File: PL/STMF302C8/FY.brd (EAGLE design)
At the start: 70 x 69 mm, 51 parts, among them J1 CON-SD-CARD_MICROSD-2908-05, J2 Flash Programming, U1 AS72652-BLGT, U2 AS72653-BLGT, U3 STM32F302C8T6, U4 AS72651-BLGT, U5 AMS1117-3.3, U6 4MB Flash, Y2 ABM2B-8.000MHZ-10-1-U-T

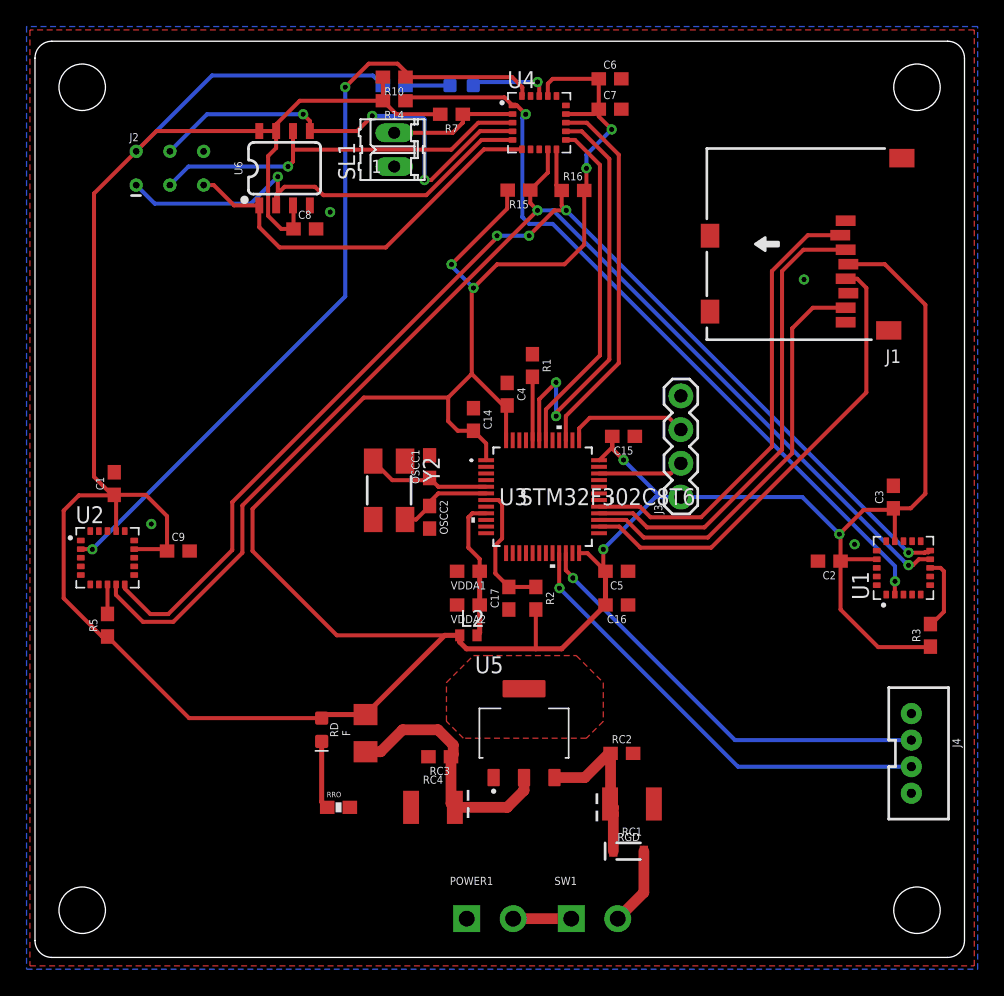
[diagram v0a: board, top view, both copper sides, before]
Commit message: Connector was changed and Preparing first order
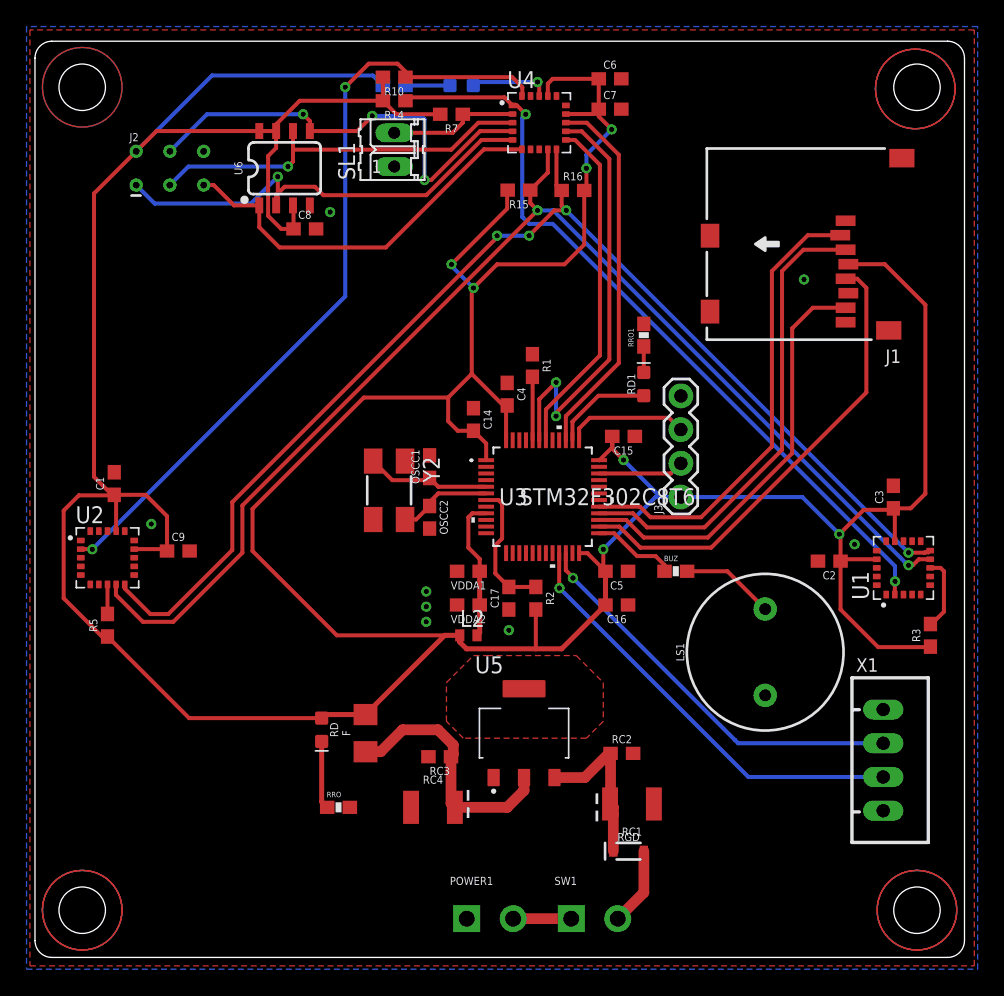
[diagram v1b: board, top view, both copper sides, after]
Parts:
- removed J4: (no value), SparkFun-Connectors:JST-4-PTH-VERT
- added BUZ: 22R, SparkFun-Resistors:0603-RES
- added LS1: BUZZER-PTH, SparkFun-Electromechanical:BUZZER-12MM
- added RD1: Red, SparkFun-LED:LED-0603
- added RRO1: 1.5k, SparkFun-Resistors:0603-RES
- added X1: JST-XH-04-PIN-LONG-PAD, Rembrandt Electronics - JST XH Connectors v1-0:JST-XH-04-PACKAGE-LONG-PAD
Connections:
- new net BUZZER: BUZ.1, U3.25
- new net LED: RD1.A, U3.38
- new net N$13: BUZ.2, LS1.+
- new net N$2: RD1.C, RRO1.1
- net GND: now also LS1.-, RRO1.2, X1.1, X1.4; no longer J4.1, J4.4
- net RX_T: now also X1.3; no longer J4.3
- net TX_T: now also X1.2; no longer J4.2
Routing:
- net LED: track 0.00 -> 7.58 mm
- net N$13: track 0.00 -> 7.06 mm
- net BUZZER: track 0.00 -> 6.39 mm
- net TX_T: track 32.6 -> 30.6 mm
- net N$2: track 0.00 -> 1.96 mm
- net RX_T: track 34.7 -> 32.9 mm
- added copper zone on layer 16, net HT1
- added copper zone on layer 1, net HT10
- added copper zone on layer 16, net HT11
- added copper zone on layer 1, net HT12
- added copper zone on layer 16, net HT13
- added copper zone on layer 1, net HT2
- added copper zone on layer 16, net HT3
- added copper zone on layer 1, net HT4
- added copper zone on layer 16, net HT5
- added copper zone on layer 1, net HT6
- added copper zone on layer 16, net HT7
- added copper zone on layer 1, net HT8
- added copper zone on layer 16, net HT9

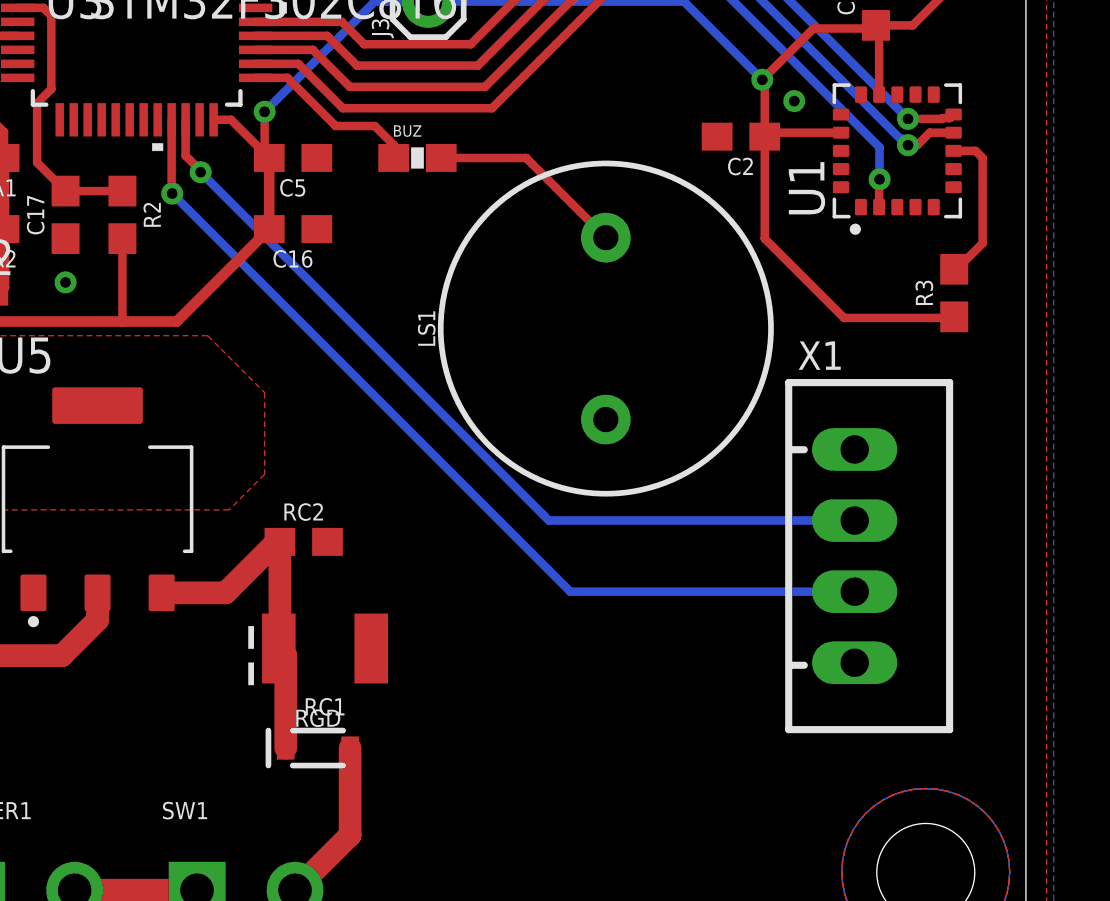
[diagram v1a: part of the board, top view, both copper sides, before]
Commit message: Polygon witdh was increased IMPOTANT**
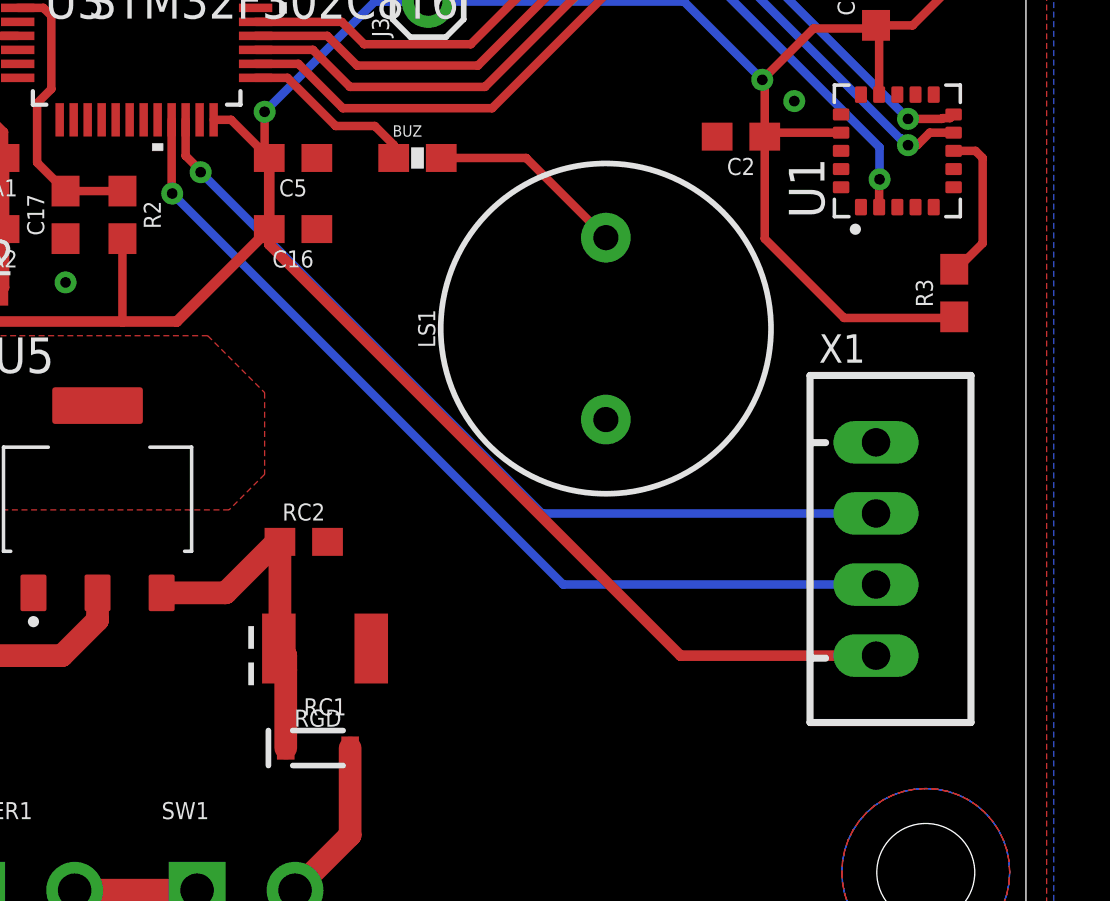
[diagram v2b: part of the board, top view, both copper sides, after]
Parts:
- moved X1 0.80 mm to (64.6, 15.1)
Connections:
- net 3.3V: now also X1.4
- net GND: no longer X1.4
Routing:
- net 3.3V: track 350.4 -> 378.7 mm
- net TX_T: track 30.6 -> 31.3 mm
- net RX_T: track 32.9 -> 33.6 mm
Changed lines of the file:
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@@
 <attribute name="VALUE" x="46.482" y="43.18" size="0.6096" layer="27" font="vector" ratio="20" rot="R90" align="top-center"/>
 </element>
-<element name="X1" library="Rembrandt Electronics - JST XH Connectors v1-0" package="JST-XH-04-PACKAGE-LONG-PAD" value="JST-XH-04-PIN-LONG-PAD" x="63.881" y="14.859" smashed="yes" rot="R270">
-<attribute name="NAME" x="61.841" y="21.514" size="1.016" layer="25" ratio="10"/>
-<attribute name="VALUE" x="67.7735" y="20.8615" size="1.016" layer="27" ratio="10" rot="R270"/>
+<element name="X1" library="Rembrandt Electronics - JST XH Connectors v1-0" package="JST-XH-04-PACKAGE-LONG-PAD" value="JST-XH-04-PIN-LONG-PAD" x="64.643" y="15.113" smashed="yes" rot="R270">
+<attribute name="NAME" x="62.603" y="21.768" size="1.016" layer="25" ratio="10"/>
+<attribute name="VALUE" x="68.5355" y="21.1155" size="1.016" layer="27" ratio="10" rot="R270"/>
 </element>
 </elements>
@@
 <contactref element="U5" pad="1"/>
 <contactref element="J1" pad="6"/>
-<polygon width="0.0762" layer="1" rank="2">
+<polygon width="0.3048" layer="1" rank="2">
 <vertex x="-0.381" y="69.85"/>
 <vertex x="-0.381" y="-0.635"/>
@@
 <vertex x="70.739" y="69.85"/>
 </polygon>
-<polygon width="0.0762" layer="16" rank="2">
+<polygon width="0.3048" layer="16" rank="2">
 <vertex x="-0.635" y="70.104"/>
 <vertex x="-0.635" y="-0.889"/>
@@
 <via x="29.464" y="26.416" extent="1-16" drill="0.381"/>
 <via x="29.464" y="25.273" extent="1-16" drill="0.381"/>
-<contactref element="X1" pad="4"/>
 <contactref element="X1" pad="1"/>
 </signal>
@@
 <wire x1="31.989" y1="24.257" x2="31.989" y2="23.749" width="0.381" layer="1"/>
 <wire x1="32.497" y1="23.241" x2="37.719" y2="23.241" width="0.381" layer="1"/>
+<contactref element="X1" pad="4"/>
+<wire x1="42.965" y1="26.543" x2="42.965" y2="25.996" width="0.381" layer="1"/>
+<wire x1="42.965" y1="25.996" x2="57.658" y2="11.303" width="0.381" layer="1"/>
+<wire x1="57.658" y1="11.303" x2="64.643" y2="11.303" width="0.381" layer="1"/>
 </signal>
 <signal name="INT">
@@
 <wire x1="39.477" y1="27.833" x2="39.477" y2="30.4464" width="0.3048" layer="1"/>
 <contactref element="X1" pad="3"/>
-<wire x1="53.721" y1="13.589" x2="63.881" y2="13.589" width="0.3048" layer="16"/>
-<wire x1="39.497" y1="27.813" x2="53.721" y2="13.589" width="0.3048" layer="16"/>
+<wire x1="53.467" y1="13.843" x2="64.643" y2="13.843" width="0.3048" layer="16"/>
+<wire x1="39.497" y1="27.813" x2="53.467" y2="13.843" width="0.3048" layer="16"/>
 </signal>
 <signal name="TX_T">
@@
 <contactref element="U3" pad="22"/>
 <wire x1="39.977" y1="29.1618" x2="39.977" y2="30.4464" width="0.3048" layer="1"/>
-<wire x1="52.721" y1="16.367" x2="52.705" y2="16.383" width="0.3048" layer="16"/>
 <contactref element="X1" pad="2"/>
-<wire x1="52.705" y1="16.383" x2="40.513" y2="28.575" width="0.3048" layer="16"/>
-<wire x1="52.721" y1="16.367" x2="52.959" y2="16.129" width="0.3048" layer="16"/>
-<wire x1="52.959" y1="16.129" x2="63.881" y2="16.129" width="0.3048" layer="16"/>
+<wire x1="52.721" y1="16.367" x2="40.513" y2="28.575" width="0.3048" layer="16"/>
+<wire x1="64.643" y1="16.383" x2="52.737" y2="16.383" width="0.3048" layer="16"/>
+<wire x1="52.721" y1="16.367" x2="52.737" y2="16.383" width="0.3048" layer="16"/>
 </signal>
 <signal name="MISO">
